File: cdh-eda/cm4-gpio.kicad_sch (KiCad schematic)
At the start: 16 parts, among them J1 THD-20-R, P1 S04B-PASK-2(LF)(SN), P2 S04B-PASK-2(LF)(SN), U1 ATA6560-GAQW-VAO, U3 MCP2510-E/SO, U4 74LVC1G07SE-7

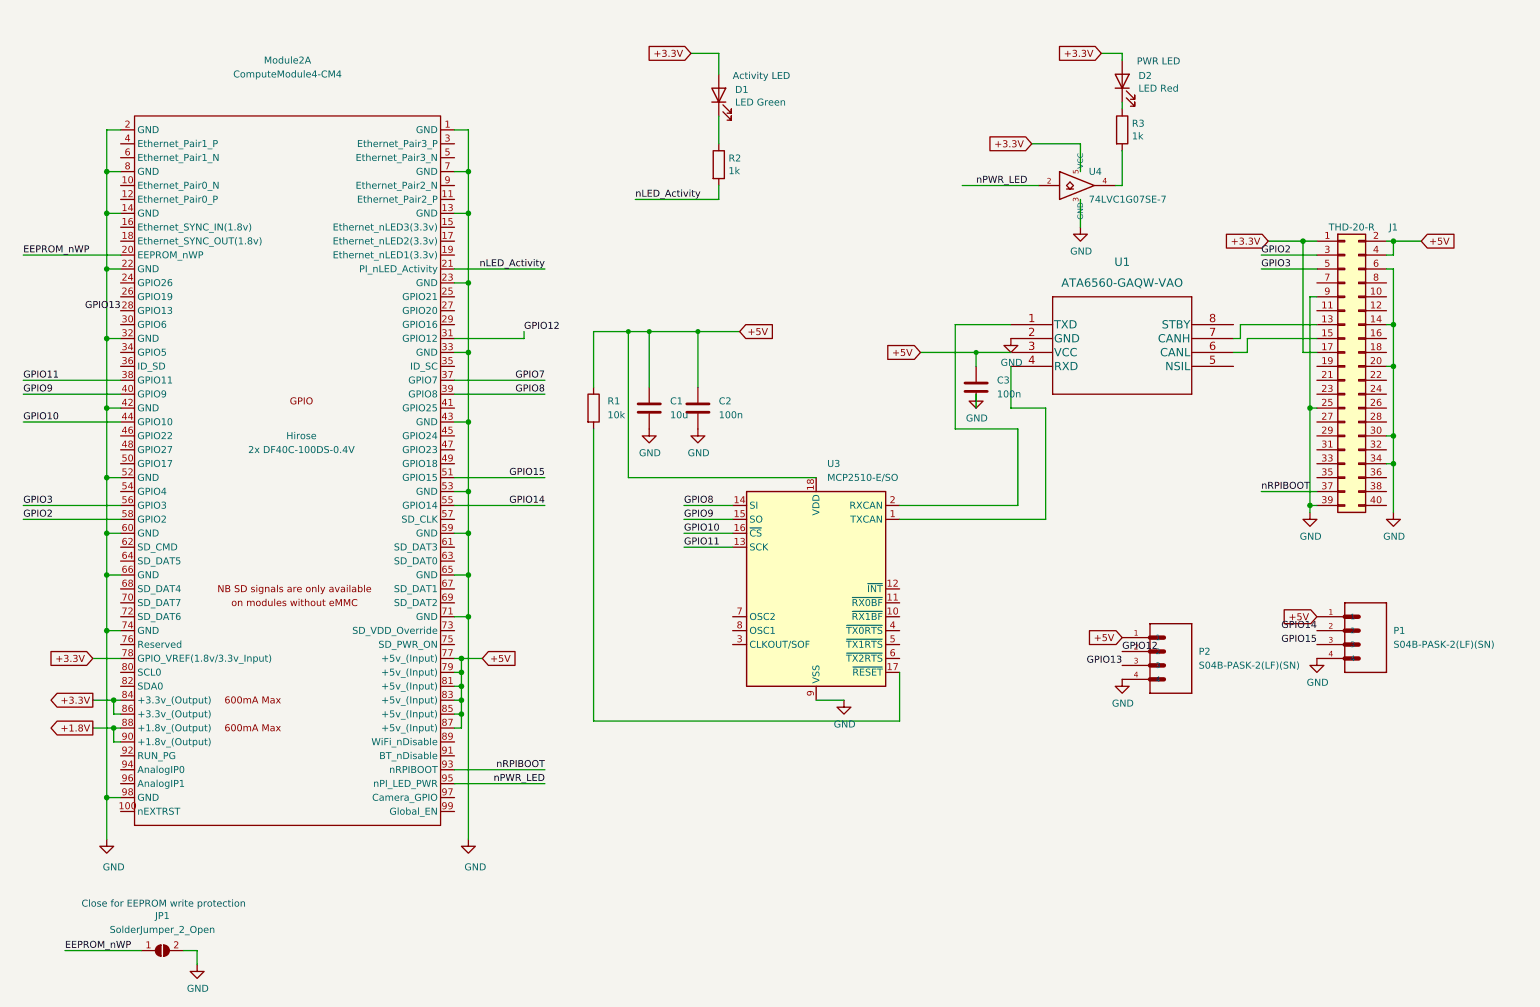
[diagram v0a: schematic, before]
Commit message: V.2 updates
 1. Add jumper CAN resistors
 2. Add camera connector
 3. Add display connector
 5. Updated CAN transceiver protective circuitry
 6. Add MCP2515 interrupt GPIO pin 18
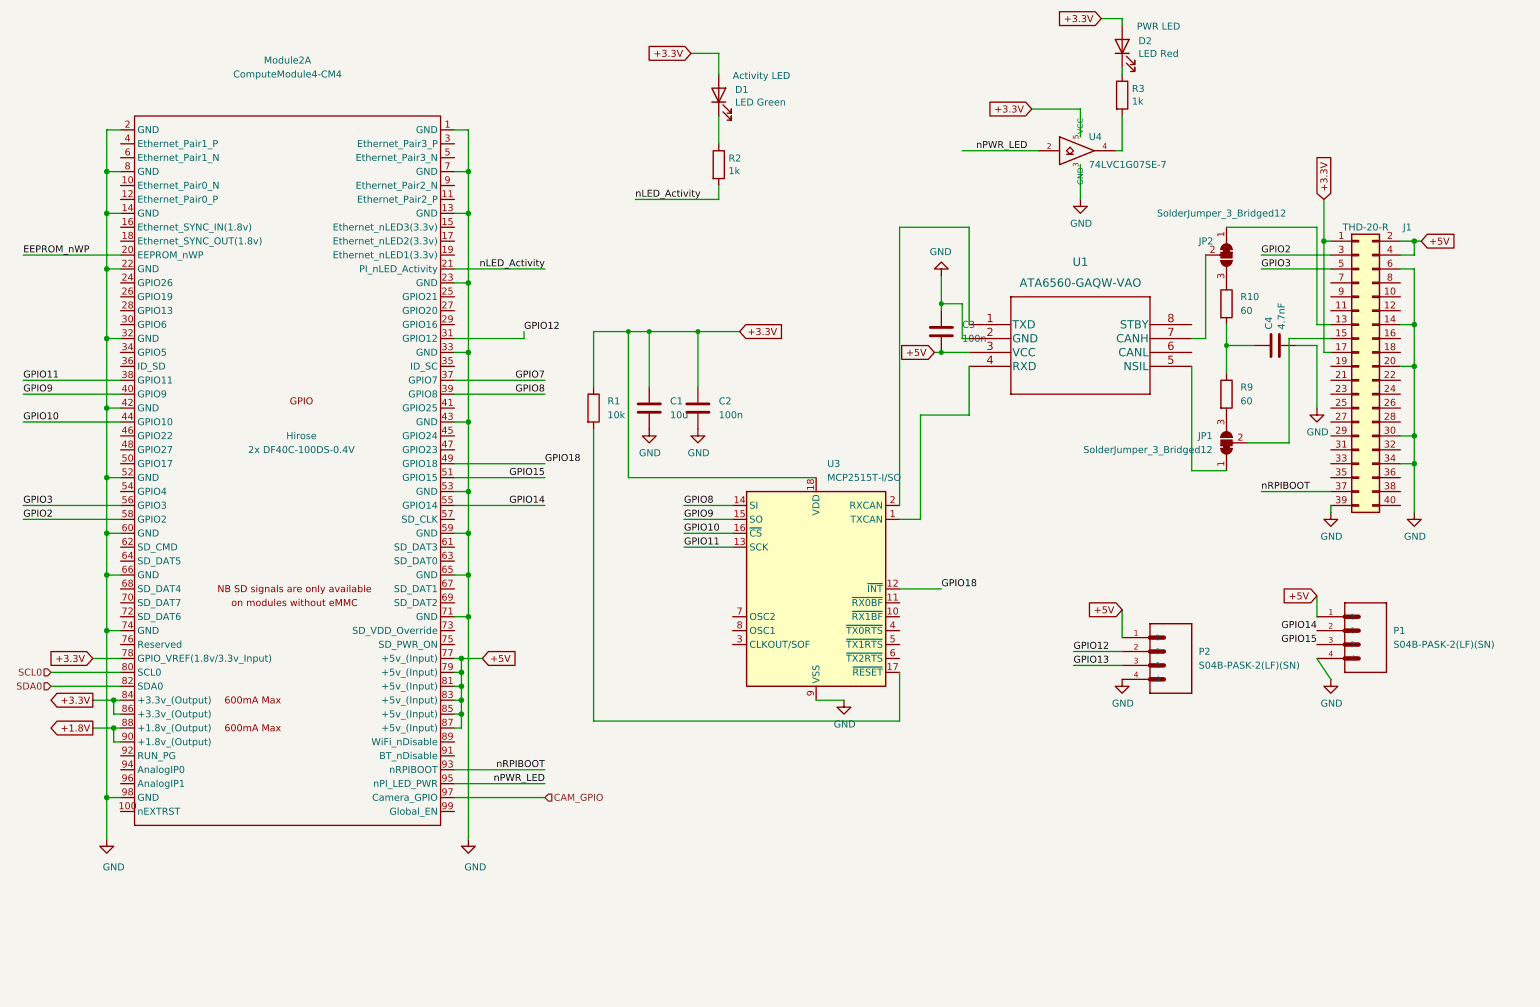
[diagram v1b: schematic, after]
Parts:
- removed JP1: SolderJumper_2_Open, Jumper:SolderJumper-2_P1.3mm_Open_RoundedPad1.0x1.5mm, symbol Jumper:SolderJumper_2_Open
- added C4: 4.7nF, Capacitor_SMD:C_0603_1608Metric, symbol Device:C
- added JP1, JP2: SolderJumper_3_Bridged12, Jumper:SolderJumper-3_P1.3mm_Bridged2Bar12_RoundedPad1.0x1.5mm, symbol Jumper:SolderJumper_3_Bridged12
- added R10, R9: 60, Resistor_SMD:R_0603_1608Metric, symbol Device:R
- U3: value MCP2510-E/SO -> MCP2515T-I/SO
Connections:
- net +3.3V: now also C1.1, C2.1, R1.1, U3.18 (VDD)
- net +5V: no longer C1.1, C2.1, R1.1, U3.18 (VDD)
- net GND: now also C4.2; no longer J1.25 (Pin_25), J1.9 (Pin_9)
- net GPIO13: no longer Module2.28 (GPIO13)
- net GPIO18: now reaches U3.12 (~{INT})
- net GPIO18: now also Module2.49 (GPIO18)
- net at U1.5 (NSIL): now also JP1.1 (A)
- net at U1.6 (CANL): no longer J1.15 (Pin_15)
- net at U1.7 (CANH): now also JP2.2 (C); no longer J1.13 (Pin_13)
- net SCL0: now reaches Module2.80 (SCL0)
- net SDA0: now reaches Module2.82 (SDA0)
- net CAM_GPIO: now reaches Module2.97 (Camera_GPIO)
- new net: C4.1, R10.2, R9.1
- new net: JP1.3 (B), R9.2
- new net: J1.13 (Pin_13), JP2.1 (A)
- new net: JP2.3 (B), R10.1
- new net: J1.15 (Pin_15), JP1.2 (C)
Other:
- note removed: "Close for EEPROM write protection"
- moved on the sheet: D2, J1, R3, U1, U4
